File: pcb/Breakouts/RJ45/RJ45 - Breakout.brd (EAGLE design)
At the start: 45 x 51 mm, 9 parts, among them X2 RJ45-8X

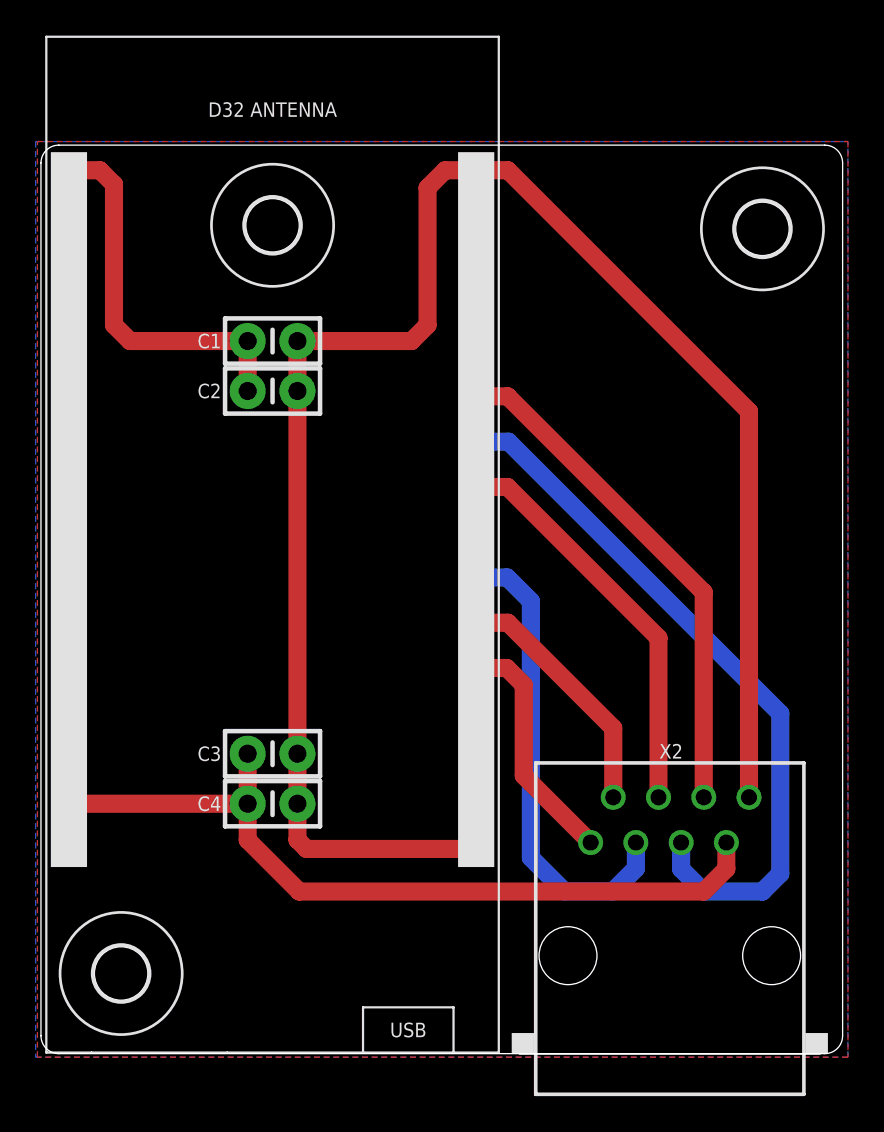
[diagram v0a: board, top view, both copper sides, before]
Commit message: Rewire, move to 9 meters
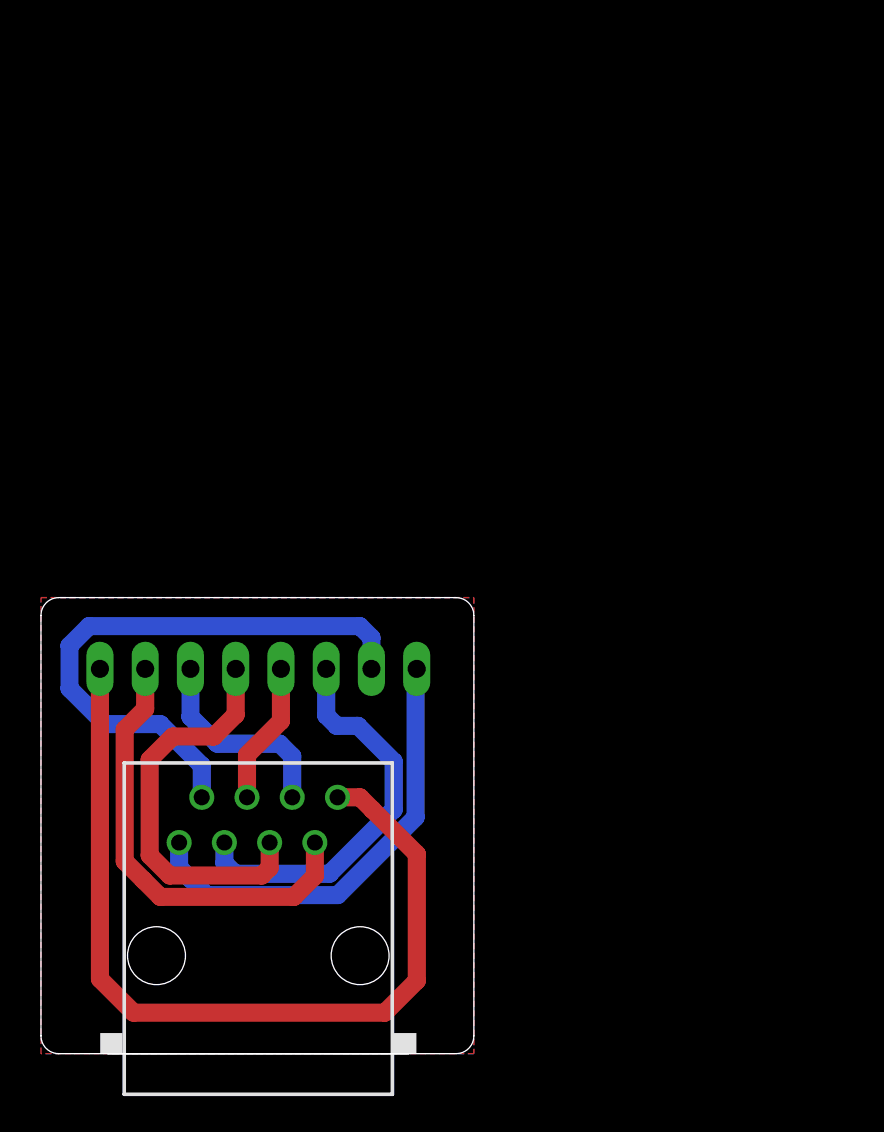
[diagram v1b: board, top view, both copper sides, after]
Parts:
- removed C1, C3: 0.1μF, Donnie:CAP_PTH-2.54
- removed C2, C4: 1.0μF, Donnie:CAP_PTH-2.54
- removed D32: Lolin D32, Donnie:D32_NO_BATT
- removed U$1, U$2, U$3: (no value), holes:3,0
- removed X2: RJ45-8X, con-tycoelectronics:RJ45-NO-SHIELD
- added IN: RJ45-8X, con-tycoelectronics:RJ45-NO-SHIELD
- added SV1: (no value), con-lstb:MA08-1
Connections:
- removed net 5V: C3.1, C4.1, D32.VBUS, X2.7
- removed net GND: C1.2, C2.2, C3.2, C4.2, D32.GND, D32.GND2, X2.8
- removed net KEG1: D32.IO4, X2.1
- removed net KEG2: D32.IO16, X2.2
- removed net KEG3: D32.IO17, X2.3
- removed net KEG4: D32.IO18, X2.4
- removed net KEG5: D32.IO19, X2.5
- removed net KEG6: D32.IO21, X2.6
- removed net VCC: C1.1, C2.1, D32.VCC
- new net 1: IN.1, SV1.1
- new net 2: IN.2, SV1.2
- new net 3: IN.3, SV1.3
- new net 4: IN.4, SV1.4
- new net 5: IN.5, SV1.5
- new net 6: IN.6, SV1.6
- new net 7: IN.7, SV1.7
- new net 8: IN.8, SV1.8
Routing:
- net GND: track 99.3 -> 0.00 mm
- net 8: track 0.00 -> 49.6 mm
- net 5V: track 44.9 -> 0.00 mm
- net KEG5: track 40.4 -> 0.00 mm
- net 2: track 0.00 -> 32.8 mm
- net KEG6: track 28.8 -> 0.00 mm
- net KEG3: track 26.7 -> 0.00 mm
- net 1: track 0.00 -> 25.5 mm
- net 7: track 0.00 -> 25.1 mm
- net KEG4: track 22.7 -> 0.00 mm
- net 5: track 0.00 -> 22.6 mm
- net 3: track 0.00 -> 22.6 mm
- net VCC: track 21.4 -> 0.00 mm
- net KEG2: track 14.0 -> 0.00 mm
- net KEG1: track 13.5 -> 0.00 mm
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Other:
- board size 45 x 51 mm -> 24.3 x 25.6 mm
- board text removed: "1 - KEG1 2 - KEG2 3 - KEG3 4 - KEG4"
- board text removed: "5 - KEG5 6 - KEG6 7 - 5V 8 - GND"
